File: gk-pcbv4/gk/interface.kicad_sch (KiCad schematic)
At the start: 19 parts, among them J11 Conn_01x20, U14 TPS2051CDBV, U15 LSM6DSL

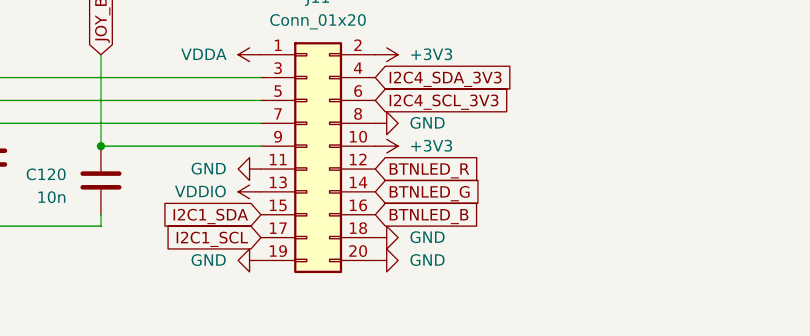
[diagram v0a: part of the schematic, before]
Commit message: add v2 controls board
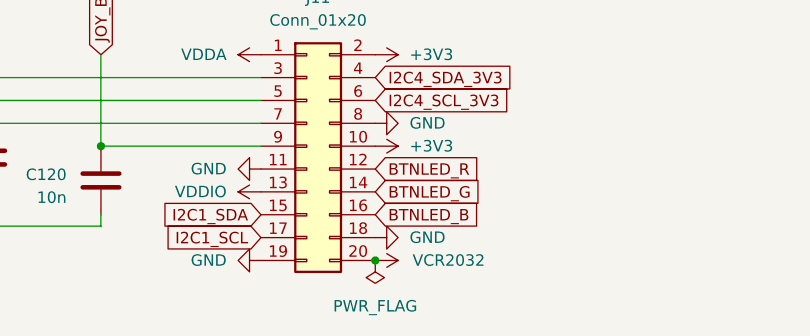
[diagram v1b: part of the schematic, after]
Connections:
- net GND: no longer J11.20 (Pin_20)
- new net VCR2032: J11.20 (Pin_20)
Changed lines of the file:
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@@
 	)
 	(junction
+		(at 154.94 187.96)
+		(diameter 0)
+		(color 0 0 0 0)
+	)
+	(junction
 		(at 231.14 48.26)
 		(diameter 0)
@@
 	(symbol
 		(lib_id "power:VDD")
+		(at 154.94 187.96 270)
+		(unit 1)
+		(exclude_from_sim no)
+		(in_bom yes)
+		(on_board yes)
+		(dnp no)
+		(property "Reference" "#PWR0107"
+			(at 151.13 187.96 0)
+			(effects
+				(font
+					(size 1.27 1.27)
+				)
+				(hide yes)
+			)
+		)
+		(property "Value" "VCR2032"
+			(at 167.132 187.96 90)
+			(effects
+				(font
+					(size 1.27 1.27)
+				)
+				(justify right)
+			)
+		)
+		(property "Footprint" ""
+			(at 154.94 187.96 0)
+			(effects
+				(font
+					(size 1.27 1.27)
+				)
+				(hide yes)
+			)
+		)
+		(property "Datasheet" ""
+			(at 154.94 187.96 0)
+			(effects
+				(font
+					(size 1.27 1.27)
+				)
+				(hide yes)
+			)
+		)
+		(property "Description" "Power symbol creates a global label with name \"VDD\""
+			(at 154.94 187.96 0)
+			(effects
+				(font
+					(size 1.27 1.27)
+				)
+				(hide yes)
+			)
+		)
+		(pin "1"
+		)
+		(instances
+			(project "gk"
+				(path "/a049c72e-5361-408c-ab21-661d491fee9d/49d92768-2753-4845-8f5d-30a44b61f9f1"
+					(reference "#PWR0107")
+					(unit 1)
+				)
+			)
+		)
+	)
+	(symbol
+		(lib_id "power:VDD")
 		(at 142.24 180.34 90)
 		(unit 1)
@@
 	)
 	(symbol
-		(lib_id "power:GND")
-		(at 154.94 187.96 90)
-		(mirror x)
-		(unit 1)
-		(exclude_from_sim no)
-		(in_bom yes)
-		(on_board yes)
-		(dnp no)
-		(fields_autoplaced yes)
-		(property "Reference" "#PWR0350"
-			(at 161.29 187.96 0)
-			(effects
-				(font
-					(size 1.27 1.27)
-				)
-				(hide yes)
-			)
-		)
-		(property "Value" "GND"
-			(at 158.75 187.9601 90)
-			(effects
-				(font
-					(size 1.27 1.27)
-				)
-				(justify right)
-			)
-		)
-		(property "Footprint" ""
-			(at 154.94 187.96 0)
-			(effects
-				(font
-					(size 1.27 1.27)
-				)
-				(hide yes)
-			)
-		)
-		(property "Datasheet" ""
-			(at 154.94 187.96 0)
-			(effects
-				(font
-					(size 1.27 1.27)
-				)
-				(hide yes)
-			)
-		)
-		(property "Description" "Power symbol creates a global label with name \"GND\" , ground"
-			(at 154.94 187.96 0)
-			(effects
-				(font
-					(size 1.27 1.27)
-				)
-				(hide yes)
-			)
-		)
-		(pin "1"
-		)
-		(instances
-			(project "gk"
-				(path "/a049c72e-5361-408c-ab21-661d491fee9d/49d92768-2753-4845-8f5d-30a44b61f9f1"
-					(reference "#PWR0350")
-					(unit 1)
-				)
-			)
-		)
-	)
-	(symbol
 		(lib_id "Switch:SW_Push")
 		(at 231.14 43.18 90)
@@
 					(unit 1)
 				)
+			)
+		)
+	)
+	(symbol
+		(lib_id "power:PWR_FLAG")
+		(at 154.94 187.96 180)
+		(unit 1)
+		(exclude_from_sim no)
+		(in_bom yes)
+		(on_board yes)
+		(dnp no)
+		(fields_autoplaced yes)
+		(property "Reference" "#FLG05"
+			(at 154.94 189.865 0)
+			(effects
+				(font
+					(size 1.27 1.27)
+				)
+				(hide yes)
+			)
+		)
+		(property "Value" "PWR_FLAG"
+			(at 154.94 193.04 0)
+			(effects
+				(font
+					(size 1.27 1.27)
+				)
+			)
+		)
+		(property "Footprint" ""
+			(at 154.94 187.96 0)
+			(effects
+				(font
+					(size 1.27 1.27)
+				)
+				(hide yes)
+			)
+		)
+		(property "Datasheet" "~"
+			(at 154.94 187.96 0)
+			(effects
+				(font
+					(size 1.27 1.27)
+				)
+				(hide yes)
+			)
+		)
+		(property "Description" "Special symbol for telling ERC where power comes from"
+			(at 154.94 187.96 0)
+			(effects
+				(font
+					(size 1.27 1.27)
+				)
+				(hide yes)
+			)
+		)
+		(pin "1"
+		)
+		(instances
+			(project "gk"
+				(path "/a049c72e-5361-408c-ab21-661d491fee9d/49d92768-2753-4845-8f5d-30a44b61f9f1"
+					(reference "#FLG05")
+					(unit 1)
+				)

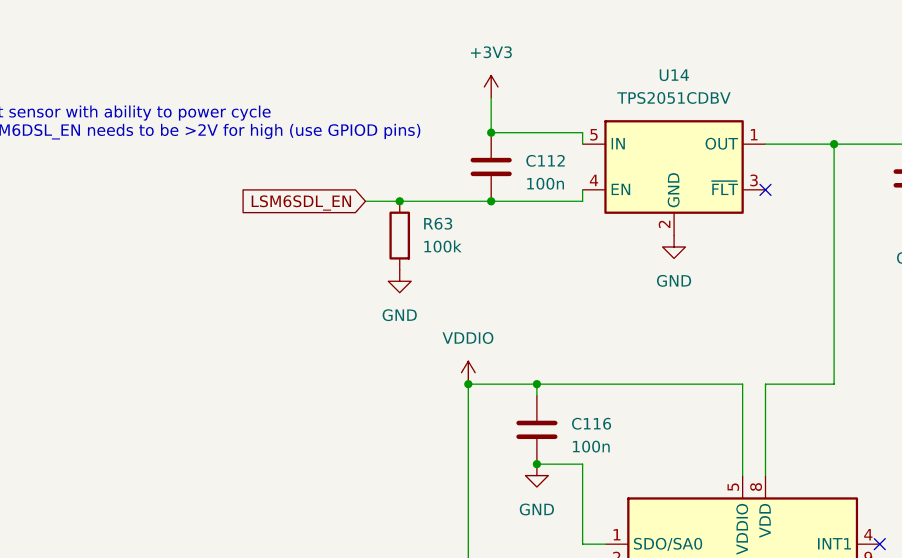
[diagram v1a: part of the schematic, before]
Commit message: fix tps2051 schematic
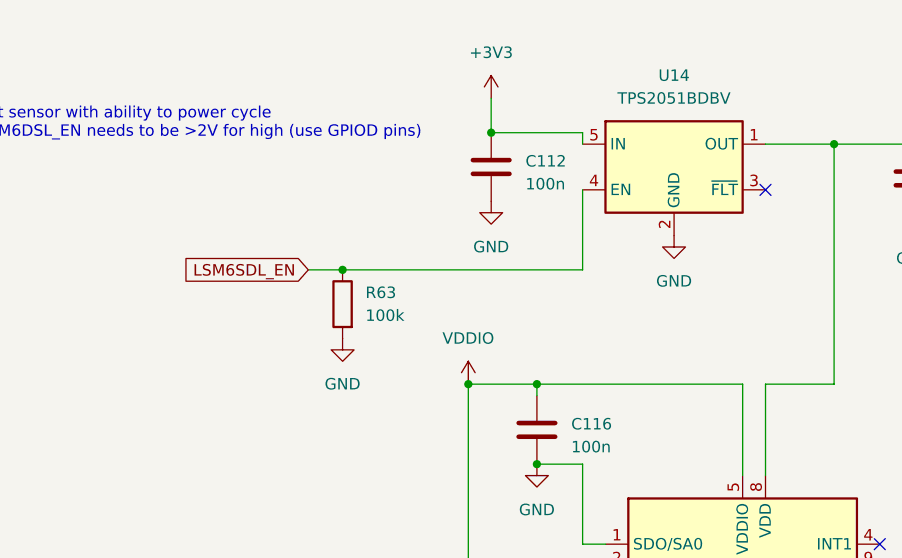
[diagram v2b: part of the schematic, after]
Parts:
- U14: value TPS2051CDBV -> TPS2051BDBV
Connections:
- net GND: now also C112.2
- net LSM6SDL_EN: no longer C112.2
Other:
- moved on the sheet: R63
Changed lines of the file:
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@@
 	)
 	(junction
-		(at 60.96 39.37)
-		(diameter 0)
-		(color 0 0 0 0)
-	)
-	(junction
 		(at 86.36 184.15)
 		(diameter 0)
@@
 	)
 	(junction
-		(at 71.12 39.37)
+		(at 231.14 36.83)
 		(diameter 0)
 		(color 0 0 0 0)
 	)
 	(junction
-		(at 231.14 36.83)
+		(at 111.76 184.15)
 		(diameter 0)
 		(color 0 0 0 0)
 	)
 	(junction
-		(at 111.76 184.15)
+		(at 54.61 46.99)
 		(diameter 0)
 		(color 0 0 0 0)
@@
 	(wire
 		(pts
-			(xy 60.96 39.37) (xy 71.12 39.37)
-		)
-		(stroke
-			(width 0)
-			(type default)
-		)
-	)
-	(wire
-		(pts
 			(xy 76.2 80.01) (xy 76.2 82.55)
 		)
@@
 	(wire
 		(pts
-			(xy 57.15 39.37) (xy 60.96 39.37)
+			(xy 50.8 46.99) (xy 54.61 46.99)
 		)
 		(stroke
@@
 	(wire
 		(pts
-			(xy 124.46 182.88) (xy 124.46 184.15)
+			(xy 54.61 46.99) (xy 81.28 46.99)
 		)
 		(stroke
@@
 	(wire
 		(pts
-			(xy 76.2 100.33) (xy 99.06 100.33)
+			(xy 124.46 182.88) (xy 124.46 184.15)
 		)
 		(stroke
@@
 	(wire
 		(pts
-			(xy 99.06 165.1) (xy 99.06 170.18)
+			(xy 76.2 100.33) (xy 99.06 100.33)
 		)
 		(stroke
@@
 	(wire
 		(pts
-			(xy 124.46 184.15) (xy 111.76 184.15)
+			(xy 99.06 165.1) (xy 99.06 170.18)
 		)
 		(stroke
@@
 	(wire
 		(pts
-			(xy 99.06 59.69) (xy 76.2 59.69)
+			(xy 124.46 184.15) (xy 111.76 184.15)
 		)
 		(stroke
@@
 	(wire
 		(pts
-			(xy 76.2 59.69) (xy 76.2 60.96)
+			(xy 99.06 59.69) (xy 76.2 59.69)
 		)
 		(stroke
@@
 	(wire
 		(pts
-			(xy 71.12 39.37) (xy 81.28 39.37)
+			(xy 76.2 59.69) (xy 76.2 60.96)
 		)
 		(stroke
@@
 	(wire
 		(pts
-			(xy 81.28 39.37) (xy 81.28 38.1)
+			(xy 81.28 38.1) (xy 81.28 46.99)
 		)
 		(stroke
@@
 	(global_label "LSM6SDL_EN"
 		(shape input)
-		(at 57.15 39.37 180)
+		(at 50.8 46.99 180)
 		(fields_autoplaced yes)
 		(effects
@@
 		)
 		(property "Intersheetrefs" "${INTERSHEET_REFS}"
-			(at 42.3116 39.37 0)
+			(at 35.9616 46.99 0)
 			(effects
 				(font
@@
 	(symbol
 		(lib_id "power:GND")
-		(at 60.96 46.99 0)
+		(at 54.61 54.61 0)
 		(unit 1)
 		(exclude_from_sim no)
@@
 		(fields_autoplaced yes)
 		(property "Reference" "#PWR0335"
-			(at 60.96 53.34 0)
+			(at 54.61 60.96 0)
 			(effects
 				(font
@@
 		)
 		(property "Value" "GND"
-			(at 60.96 52.07 0)
+			(at 54.61 59.69 0)
 			(effects
 				(font
@@
 		)
 		(property "Footprint" ""
-			(at 60.96 46.99 0)
+			(at 54.61 54.61 0)
 			(effects
 				(font
@@
 		)
 		(property "Datasheet" ""
-			(at 60.96 46.99 0)
+			(at 54.61 54.61 0)
 			(effects
 				(font
@@
 		)
 		(property "Description" "Power symbol creates a global label with name \"GND\" , ground"
-			(at 60.96 46.99 0)
+			(at 54.61 54.61 0)
 			(effects
 				(font
@@
 	(symbol
 		(lib_id "Device:R")
-		(at 60.96 43.18 0)
+		(at 54.61 50.8 0)
 		(mirror y)
 		(unit 1)
@@
 		(fields_autoplaced yes)
 		(property "Reference" "R63"
-			(at 63.5 41.9099 0)
+			(at 57.15 49.5299 0)
 			(effects
 				(font
@@
 		)
 		(property "Value" "100k"
-			(at 63.5 44.4499 0)
+			(at 57.15 52.0699 0)
 			(effects
 				(font
@@
 		)
 		(property "Footprint" "Resistor_SMD:R_0603_1608Metric"
-			(at 62.738 43.18 90)
+			(at 56.388 50.8 90)
 			(effects
 				(font
@@
 		)
 		(property "Datasheet" "~"
-			(at 60.96 43.18 0)
+			(at 54.61 50.8 0)
 			(effects
 				(font
@@
 		)
 		(property "Description" ""
-			(at 60.96 43.18 0)
+			(at 54.61 50.8 0)
 			(effects
 				(font
@@
 			)
 		)
-		(property "Value" "TPS2051CDBV"
+		(property "Value" "TPS2051BDBV"
 			(at 91.44 27.94 0)
 			(effects
@@
 					(unit 1)
 				)
+			)
+		)
+	)
+	(symbol
+		(lib_id "power:GND")
+		(at 71.12 39.37 0)
+		(unit 1)
+		(exclude_from_sim no)
+		(in_bom yes)
+		(on_board yes)
+		(dnp no)
+		(fields_autoplaced yes)
+		(property "Reference" "#PWR040"
+			(at 71.12 45.72 0)
+			(effects
+				(font
+					(size 1.27 1.27)
+				)
+				(hide yes)
+			)
+		)
+		(property "Value" "GND"
+			(at 71.12 44.45 0)
+			(effects
+				(font
+					(size 1.27 1.27)
+				)
+			)
+		)
+		(property "Footprint" ""
+			(at 71.12 39.37 0)
+			(effects
+				(font
+					(size 1.27 1.27)
+				)
+				(hide yes)
+			)
+		)
+		(property "Datasheet" ""
+			(at 71.12 39.37 0)
+			(effects
+				(font
+					(size 1.27 1.27)
+				)
+				(hide yes)
+			)
+		)
+		(property "Description" "Power symbol creates a global label with name \"GND\" , ground"
+			(at 71.12 39.37 0)
+			(effects
+				(font
+					(size 1.27 1.27)
+				)
+				(hide yes)
+			)
+		)
+		(pin "1"
+		)
+		(instances
+			(project "gk"
+				(path "/a049c72e-5361-408c-ab21-661d491fee9d/49d92768-2753-4845-8f5d-30a44b61f9f1"
+					(reference "#PWR040")
+					(unit 1)
+				)

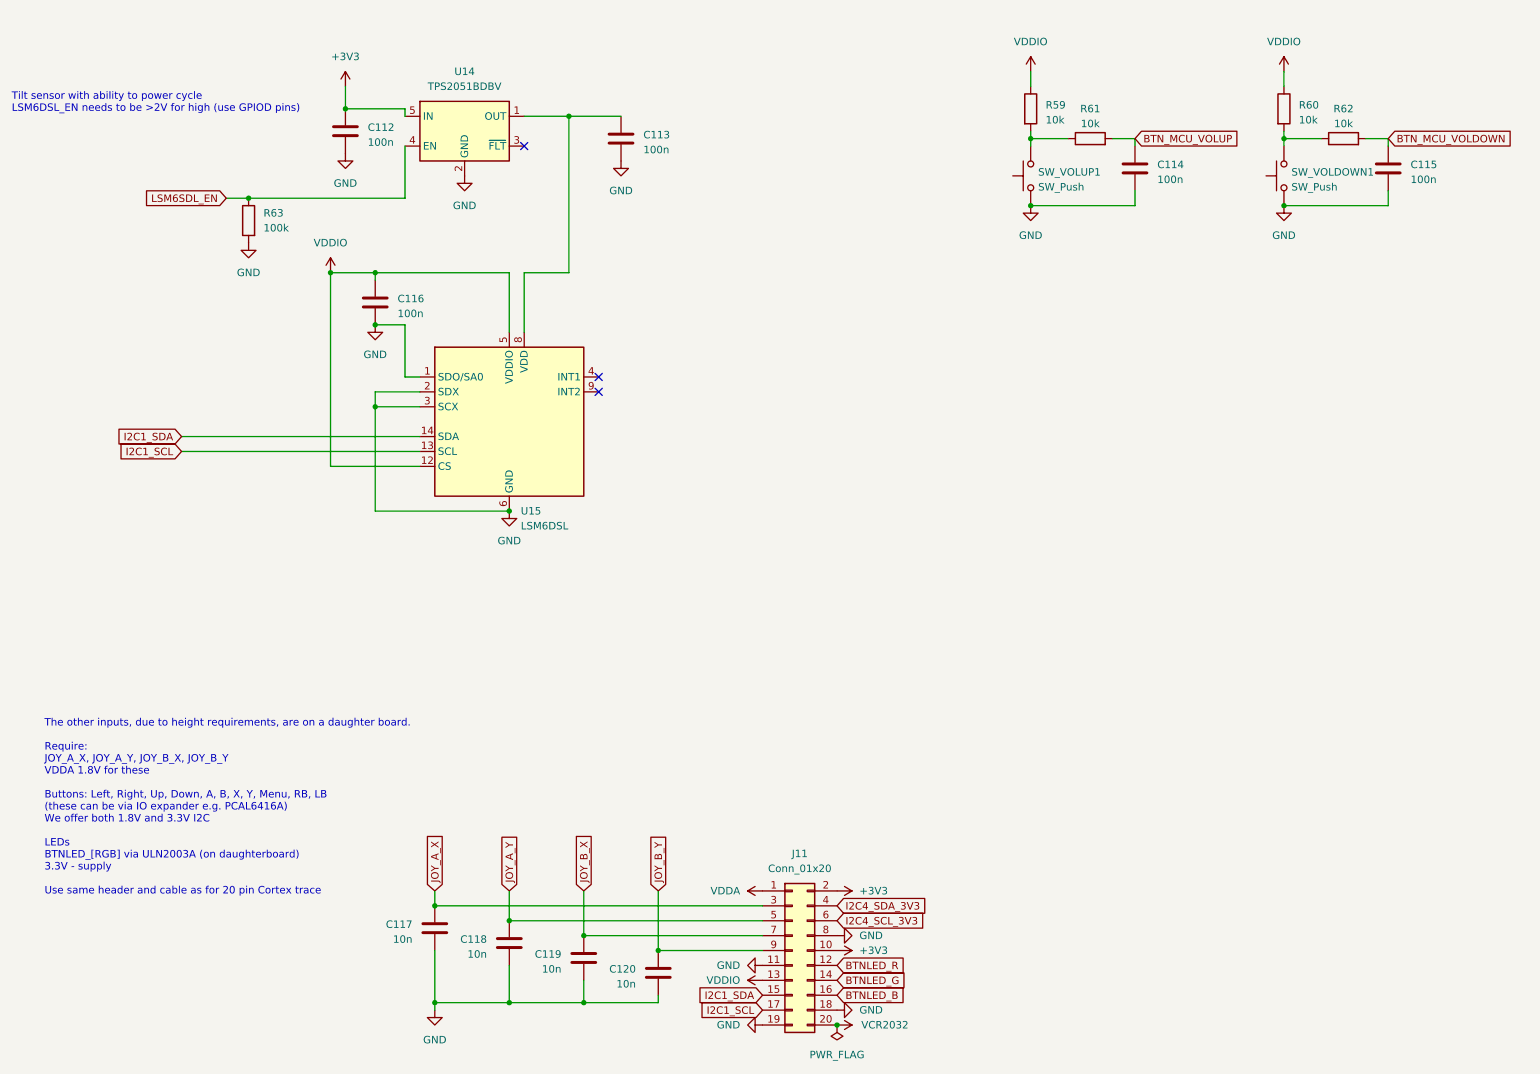
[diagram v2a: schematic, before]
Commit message: add magnetometer
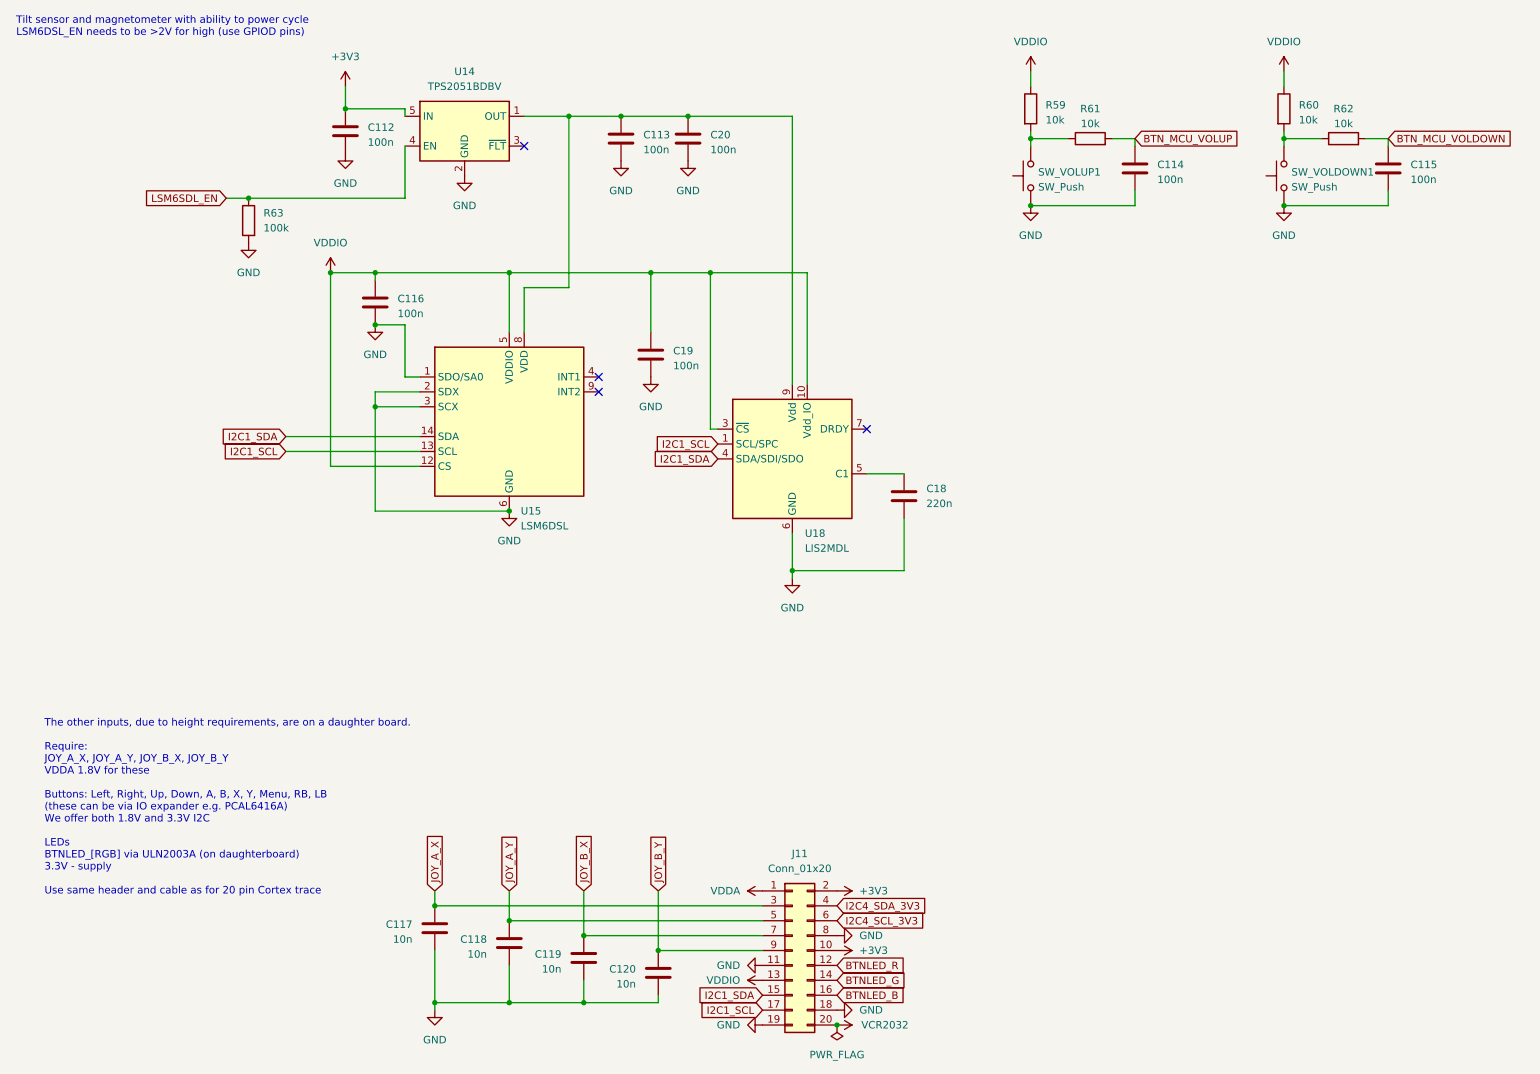
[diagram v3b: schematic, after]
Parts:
- added C18: 220n, symbol Device:C
- added C19, C20: 100n, Capacitor_SMD:C_0603_1608Metric, symbol Device:C
- added U18: LIS2MDL, Package_LGA:LGA-12_2x2mm_P0.5mm, symbol Sensor_Magnetic:LIS2MDL
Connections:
- net GND: now also C18.2, C19.2, C20.2, U18.6 (GND), U18.8 (GND)
- net I2C1_SCL: now also U18.1 (SCL/SPC)
- net I2C1_SDA: now also U18.4 (SDA/SDI/SDO)
- net VDDIO: now also C19.1, U18.10 (Vdd_IO), U18.3 (~{CS})
- net at C113.1, U14.1 (OUT), U15.8 (VDD): now also C20.1, U18.9 (Vdd)
- new net: C18.1, U18.5 (C1)
- no-connect marks 3 -> 4
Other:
- note added: "Tilt sensor and magnetometer with ability to power cycle LSM6DSL_EN needs to be >2V for high (use GPIOD pins)"
- note removed: "Tilt sensor with ability to power cycle LSM6DSL_EN needs to be >2V for high (use GPIOD pins)"

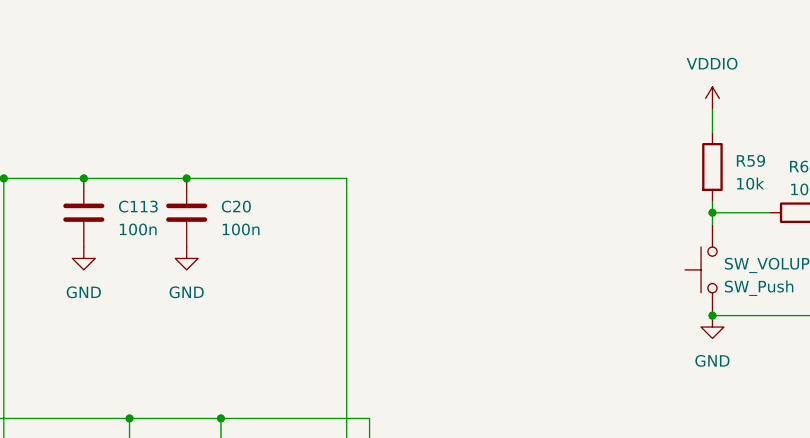
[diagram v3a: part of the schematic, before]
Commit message: add test points to power planes
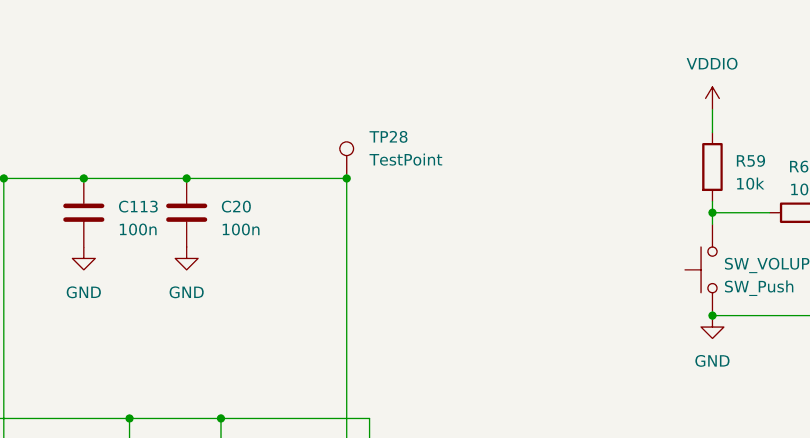
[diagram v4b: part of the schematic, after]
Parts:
- added TP28: TestPoint, TestPoint:TestPoint_Pad_D1.0mm, symbol Connector:TestPoint
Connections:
- net at C113.1, C20.1, U14.1 (OUT)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: now also TP28.1
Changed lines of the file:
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@@
 	)
 	(junction
+		(at 147.32 33.02)
+		(diameter 0)
+		(color 0 0 0 0)
+	)
+	(junction
 		(at 76.2 82.55)
 		(diameter 0)
@@
 					(unit 1)
 				)
+			)
+		)
+	)
+	(symbol
+		(lib_id "Connector:TestPoint")
+		(at 147.32 33.02 0)
+		(unit 1)
+		(exclude_from_sim no)
+		(in_bom yes)
+		(on_board yes)
+		(dnp no)
+		(fields_autoplaced yes)
+		(property "Reference" "TP28"
+			(at 149.86 28.4479 0)
+			(effects
+				(font
+					(size 1.27 1.27)
+				)
+				(justify left)
+			)
+		)
+		(property "Value" "TestPoint"
+			(at 149.86 30.9879 0)
+			(effects
+				(font
+					(size 1.27 1.27)
+				)
+				(justify left)
+			)
+		)
+		(property "Footprint" "TestPoint:TestPoint_Pad_D1.0mm"
+			(at 152.4 33.02 0)
+			(effects
+				(font
+					(size 1.27 1.27)
+				)
+				(hide yes)
+			)
+		)
+		(property "Datasheet" "~"
+			(at 152.4 33.02 0)
+			(effects
+				(font
+					(size 1.27 1.27)
+				)
+				(hide yes)
+			)
+		)
+		(property "Description" "test point"
+			(at 147.32 33.02 0)
+			(effects
+				(font
+					(size 1.27 1.27)
+				)
+				(hide yes)
+			)
+		)
+		(pin "1"
+		)
+		(instances
+			(project "gk"
+				(path "/a049c72e-5361-408c-ab21-661d491fee9d/49d92768-2753-4845-8f5d-30a44b61f9f1"
+					(reference "TP28")
+					(unit 1)
+				)

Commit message: Add throttle control
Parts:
- added C28: 10n, Capacitor_SMD:C_0603_1608Metric, symbol Device:C
- added RV1: R_Potentiometer, gk-pcbv3:Alps_RK10J11R0A0L, symbol Device:R_Potentiometer
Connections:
- net GND: now also C28.2, RV1.3
- net VDDA: now also RV1.1
- new net JOY_THROTTLE: C28.1, RV1.2
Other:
- note added: "Throttle style control"
